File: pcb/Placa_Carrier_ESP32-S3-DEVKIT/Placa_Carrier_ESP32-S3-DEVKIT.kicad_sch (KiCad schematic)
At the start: 41 parts, among them J1 12V IN, J2 AN_IN, J3 RELE, J4 CAN, J5 DevKit_J1, J6 DevKit_J3, J7 EXP_J1, J8 EXP_J3, K1 SRD-05VDC, Q1 BC817, SW1 SW_Push, SW2 SW_Push, U1 AMS1117-ADJ, U3 MCP2562-E-SN

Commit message: Actualiza sch
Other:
- note removed: "Si conmuta 220 V: aislar la zona de contactos en el PCB."
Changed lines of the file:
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@@
-		)
-	)
-	(text "Si conmuta 220 V: aislar la zona de contactos en el PCB."
-		(exclude_from_sim no)
-		(at 285.75 128.27 0)
-		(effects
-			(font
-				(size 1.27 1.27)
-			)
-			(justify left bottom)
 		)
 	)
@@
 	(text "EXPANSIÓN (tiras hembra en paralelo con J5 / J6)"
 		(exclude_from_sim no)
-		(at 38.1 194.31 0)
+		(at 53.848 194.056 0)
 		(effects
 			(font
@@
 	(text "- Verificar la separación entre tiras con el plano de la DevKit antes del PCB."
 		(exclude_from_sim no)
-		(at 38.1 182.88 0)
+		(at 54.864 180.594 0)
 		(effects
 			(font
@@
 	(text "1: COM  2: NA  3: NC"
 		(exclude_from_sim no)
-		(at 360.68 77.47 0)
+		(at 360.934 77.216 0)
 		(effects
 			(font
@@
 	(text "- GPIO0, 3, 45, 46: strapping. GPIO19/20: USB nativo. GPIO43/44: UART0."
 		(exclude_from_sim no)
-		(at 38.1 177.8 0)
+		(at 54.864 175.514 0)
 		(effects
 			(font
@@
 	(text "- LED RGB de la placa: GPIO48 (v1.0) / GPIO38 (v1.1). No usados acá."
 		(exclude_from_sim no)
-		(at 38.1 175.26 0)
+		(at 54.864 172.974 0)
 		(effects
 			(font
@@
 	(text "Notas DevKit:"
 		(exclude_from_sim no)
-		(at 38.1 171.45 0)
+		(at 54.864 169.164 0)
 		(effects
 			(font
@@
 	(text "- GPIO35-37: PSRAM octal en módulos N8R8/N16R8. AN1 en GPIO1 (ADC1)."
 		(exclude_from_sim no)
-		(at 38.1 180.34 0)
-		(effects
-			(font
+		(at 54.864 178.054 0)
+		(effects
+			(font

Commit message: Empieza a cambiar hoja a A4
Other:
- moved on the sheet: C1, C2, C3, C4, C5, C6, D1, D2, D3, D4, D5, D6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

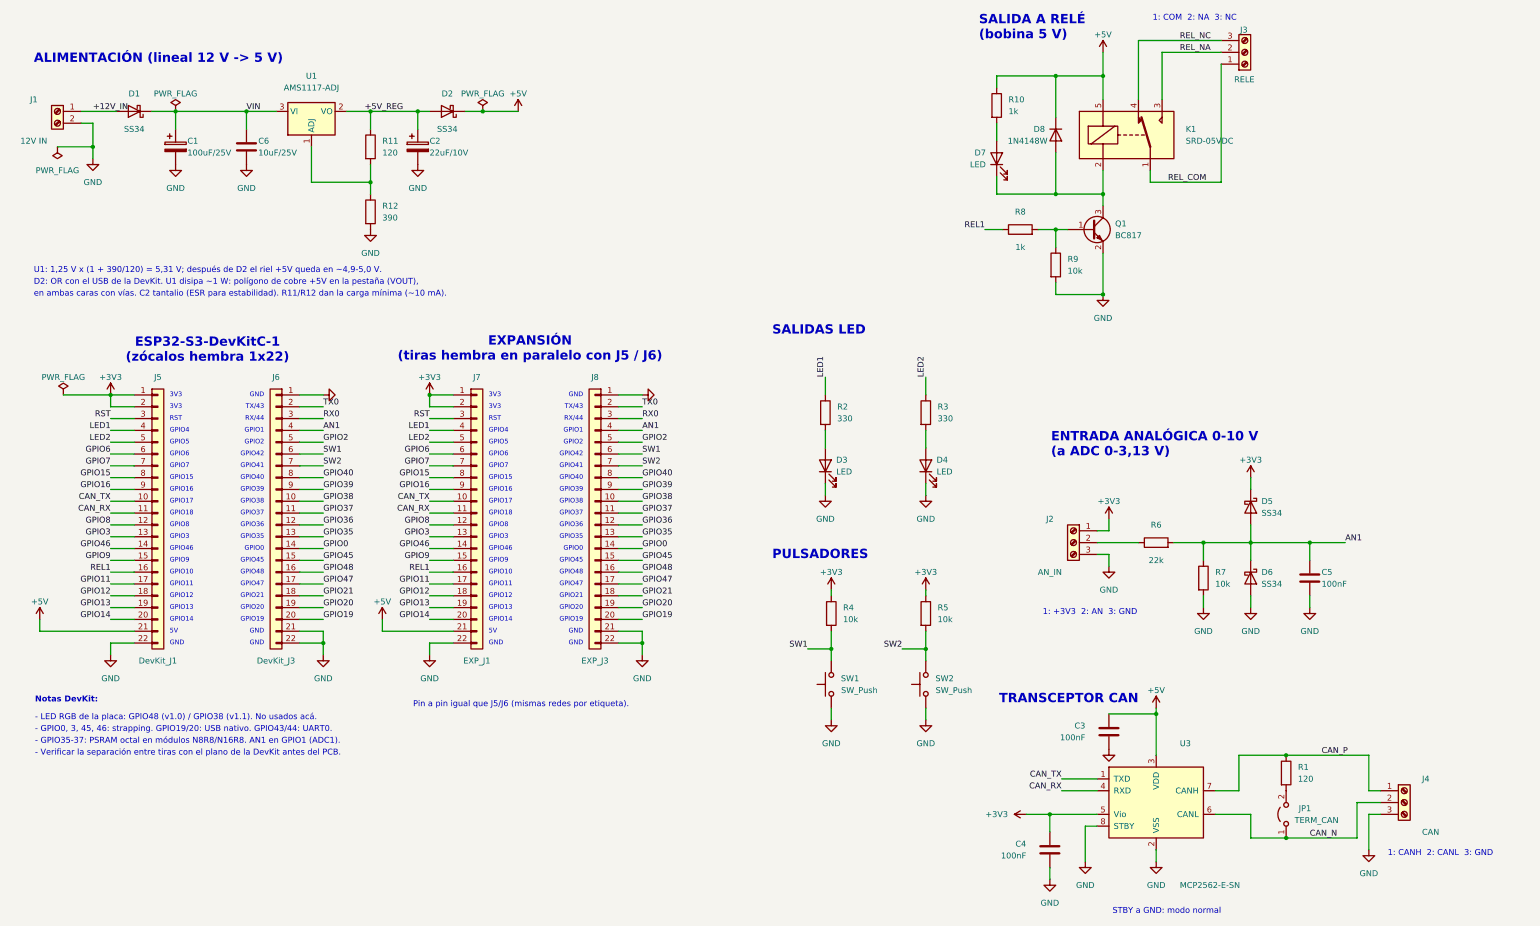
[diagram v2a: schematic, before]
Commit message: Hoja de sch pasada a A4
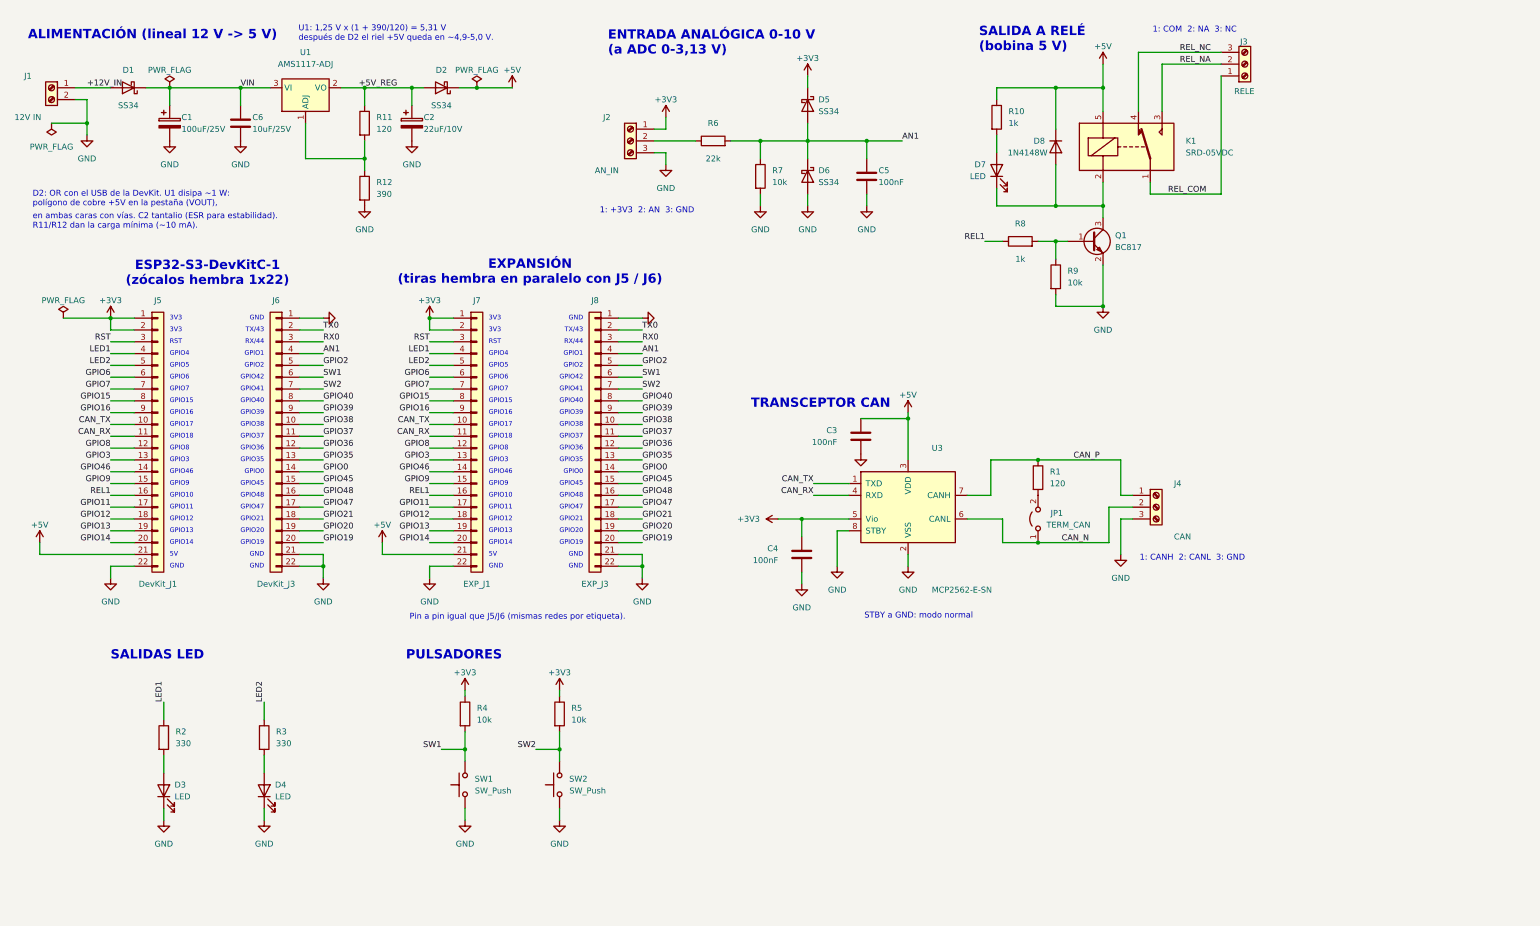
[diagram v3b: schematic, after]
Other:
- note added: "U1: 1,25 V x (1 + 390/120) = 5,31 V después de D2 el riel +5V queda en ~4,9-5,0 V."
- note removed: "- GPIO0, 3, 45, 46: strapping. GPIO19/20: USB nativo. GPIO43/44: UART0."
- note removed: "- GPIO35-37: PSRAM octal en módulos N8R8/N16R8. AN1 en GPIO1 (ADC1)."
- note removed: "- LED RGB de la placa: GPIO48 (v1.0) / GPIO38 (v1.1). No usados acá."
- note removed: "- Verificar la separación entre tiras con el plano de la DevKit antes del PCB."
- note removed: "Notas DevKit:"
- note removed: "U1: 1,25 V x (1 + 390/120) = 5,31 V; después de D2 el riel +5V queda en ~4,9-5,0 V."
- moved on the sheet: C1, C2, C5, C6, D1, D2, D3, D4, D5, D6, D7, D8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
